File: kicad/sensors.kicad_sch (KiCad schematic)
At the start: 11 parts, among them U10 BMM350, U11 BMP581, U9 ICM-45686

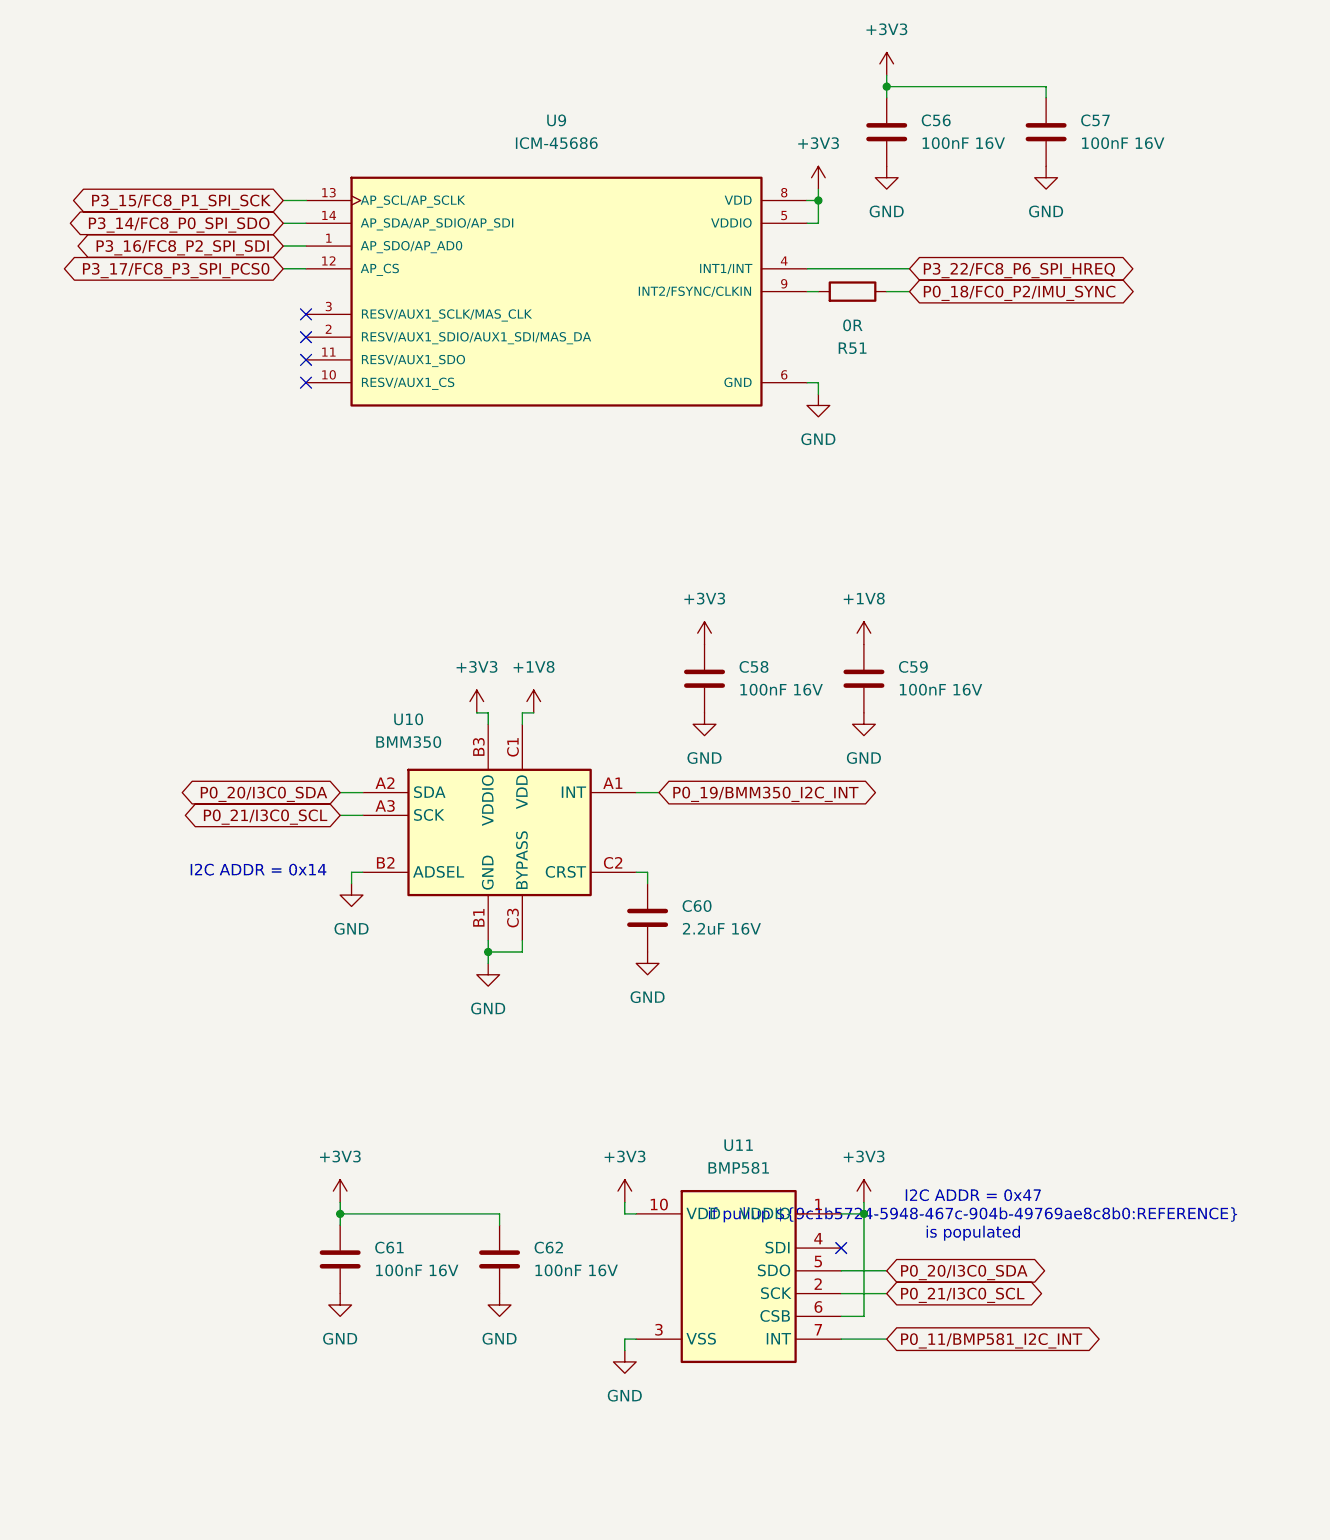
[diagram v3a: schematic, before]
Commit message: Finished schematic. Completed power and ENET phy layout.
Layouted power supply and ethernet phy around input connector.
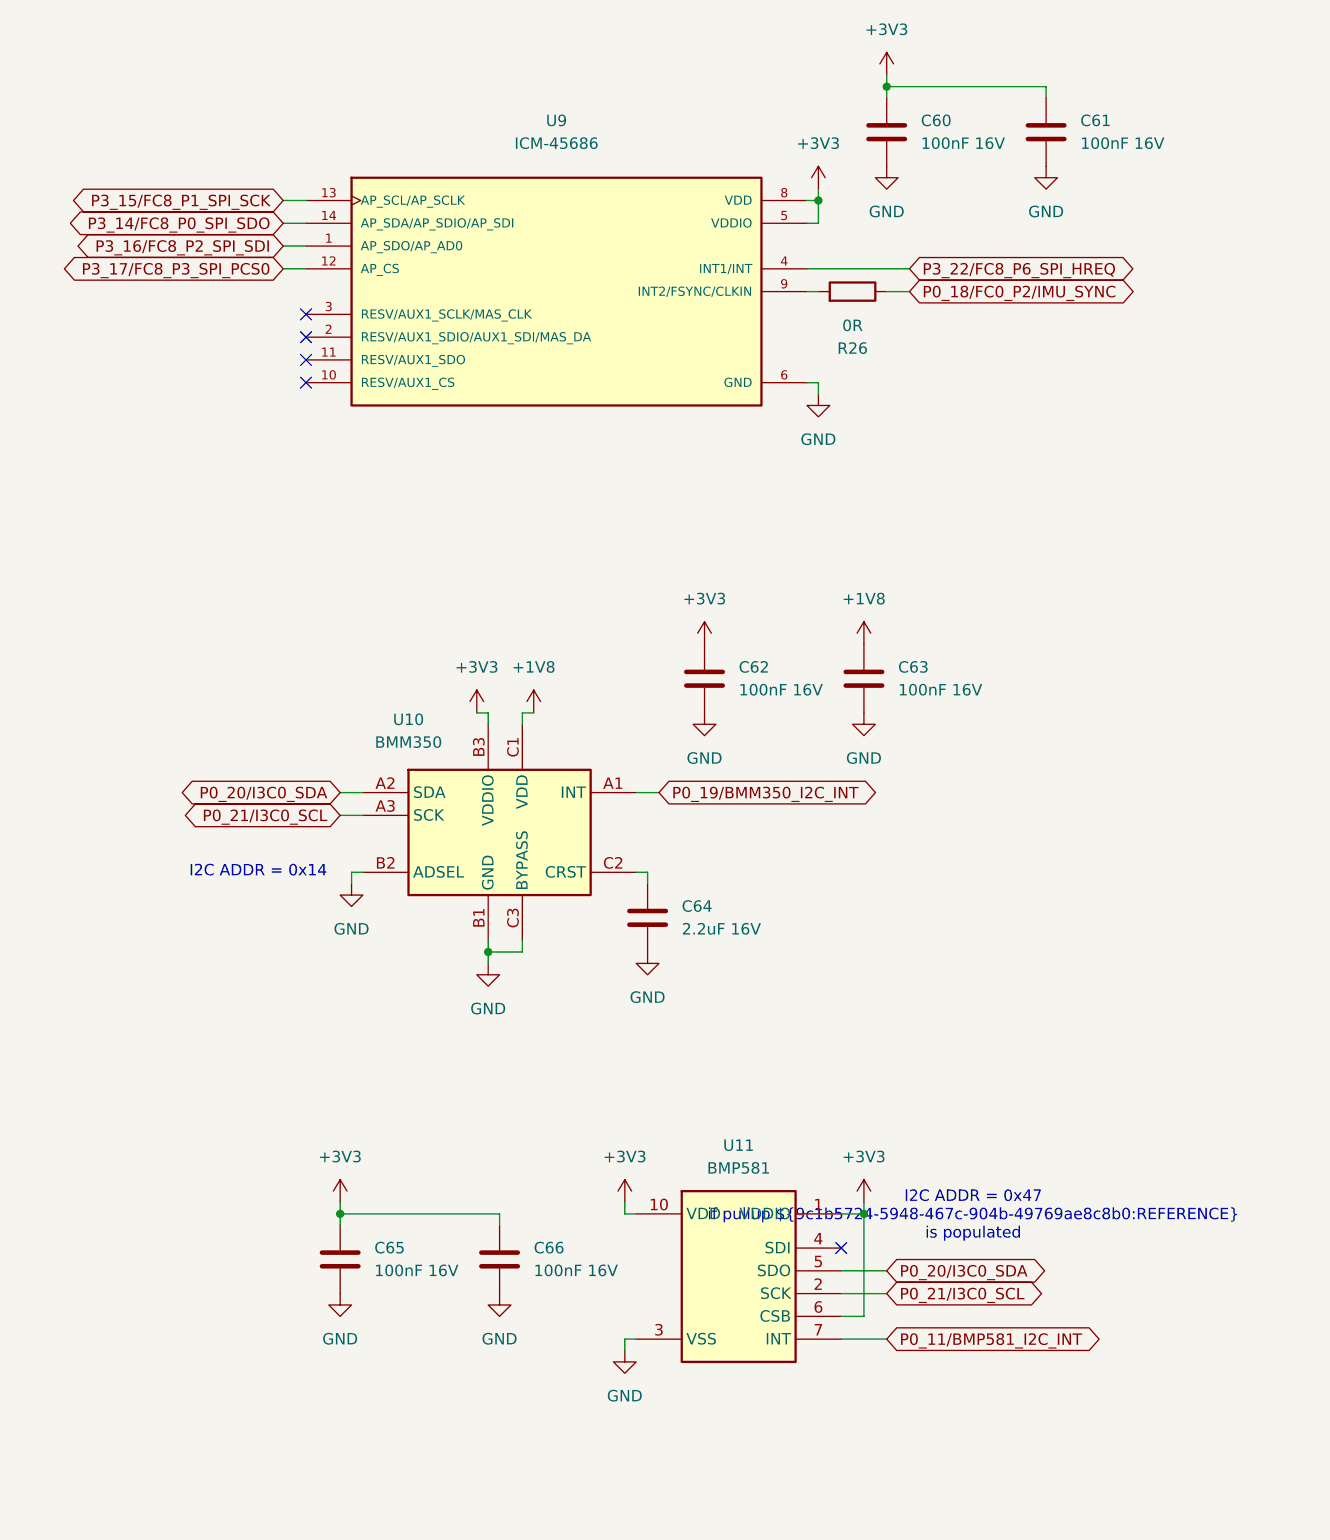
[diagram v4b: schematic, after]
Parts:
- R26: renamed from R51; footprint (none) -> Resistor_SMD:R_0402_1005Metric; MF (none) -> YAGEO; MFPN (none) -> RC0402JR-070RL; Supplier (none) -> JLCPCB; Supplier PN (none) -> C60485
- renumbered C56 to C60, C57 to C61, C58 to C62, C59 to C63, C60 to C64, C61 to C65, C62 to C66
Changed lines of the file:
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@@
 		(dnp no)
 		(fields_autoplaced yes)
-		(property "Reference" "#PWR0119"
+		(property "Reference" "#PWR0121"
 			(at 88.9 162.56 0)
 			(effects
@@
 			(project ""
 				(path "/8b469ec1-e800-4d46-8a32-95d77ceae6db/a28c0fd8-aeac-4bef-8f3f-cec5db09a131"
-					(reference "#PWR0119")
+					(reference "#PWR0121")
 					(unit 1)
 				)
@@
 		(dnp no)
 		(fields_autoplaced yes)
-		(property "Reference" "#PWR0105"
+		(property "Reference" "#PWR0107"
 			(at 118.11 49.53 0)
 			(effects
@@
 			(project "spinali_mcxn_t1_sensor_hub"
 				(path "/8b469ec1-e800-4d46-8a32-95d77ceae6db/a28c0fd8-aeac-4bef-8f3f-cec5db09a131"
-					(reference "#PWR0105")
+					(reference "#PWR0107")
 					(unit 1)
 				)
@@
 		(dnp no)
 		(fields_autoplaced yes)
-		(property "Reference" "#PWR0107"
+		(property "Reference" "#PWR0109"
 			(at 110.49 49.53 0)
 			(effects
@@
 			(project ""
 				(path "/8b469ec1-e800-4d46-8a32-95d77ceae6db/a28c0fd8-aeac-4bef-8f3f-cec5db09a131"
-					(reference "#PWR0107")
+					(reference "#PWR0109")
 					(unit 1)
 				)
@@
 		(dnp no)
 		(fields_autoplaced yes)
-		(property "Reference" "#PWR0116"
+		(property "Reference" "#PWR0118"
 			(at 91.44 137.16 0)
 			(effects
@@
 			(project "spinali_mcxn_t1_sensor_hub"
 				(path "/8b469ec1-e800-4d46-8a32-95d77ceae6db/a28c0fd8-aeac-4bef-8f3f-cec5db09a131"
-					(reference "#PWR0116")
+					(reference "#PWR0118")
 					(unit 1)
 				)
@@
 		(dnp no)
 		(fields_autoplaced yes)
-		(property "Reference" "#PWR0108"
+		(property "Reference" "#PWR0110"
 			(at 110.49 74.93 0)
 			(effects
@@
 			(project "spinali_mcxn_t1_sensor_hub"
 				(path "/8b469ec1-e800-4d46-8a32-95d77ceae6db/a28c0fd8-aeac-4bef-8f3f-cec5db09a131"
-					(reference "#PWR0108")
+					(reference "#PWR0110")
 					(unit 1)
 				)
@@
 		(dnp no)
 		(fields_autoplaced yes)
-		(property "Reference" "C60"
+		(property "Reference" "C64"
 			(at 95.25 125.7299 0)
 			(effects
@@
 			(project "spinali_mcxn_t1_sensor_hub"
 				(path "/8b469ec1-e800-4d46-8a32-95d77ceae6db/a28c0fd8-aeac-4bef-8f3f-cec5db09a131"
-					(reference "C60")
+					(reference "C64")
 					(unit 1)
 				)
@@
 		(dnp no)
 		(fields_autoplaced yes)
-		(property "Reference" "C59"
+		(property "Reference" "C63"
 			(at 119.38 99.0599 0)
 			(effects
@@
 			(project "spinali_mcxn_t1_sensor_hub"
 				(path "/8b469ec1-e800-4d46-8a32-95d77ceae6db/a28c0fd8-aeac-4bef-8f3f-cec5db09a131"
-					(reference "C59")
+					(reference "C63")
 					(unit 1)
 				)
@@
 		(dnp no)
 		(fields_autoplaced yes)
-		(property "Reference" "C57"
+		(property "Reference" "C61"
 			(at 139.7 38.0999 0)
 			(effects
@@
 			(project "spinali_mcxn_t1_sensor_hub"
 				(path "/8b469ec1-e800-4d46-8a32-95d77ceae6db/a28c0fd8-aeac-4bef-8f3f-cec5db09a131"
-					(reference "C57")
+					(reference "C61")
 					(unit 1)
 				)
@@
 		(dnp no)
 		(fields_autoplaced yes)
-		(property "Reference" "#PWR0113"
+		(property "Reference" "#PWR0115"
 			(at 97.79 110.49 0)
 			(effects
@@
 			(project "spinali_mcxn_t1_sensor_hub"
 				(path "/8b469ec1-e800-4d46-8a32-95d77ceae6db/a28c0fd8-aeac-4bef-8f3f-cec5db09a131"
-					(reference "#PWR0113")
+					(reference "#PWR0115")
 					(unit 1)
 				)
@@
 		(dnp no)
 		(fields_autoplaced yes)
-		(property "Reference" "#PWR0106"
+		(property "Reference" "#PWR0108"
 			(at 135.89 49.53 0)
 			(effects
@@
 			(project "spinali_mcxn_t1_sensor_hub"
 				(path "/8b469ec1-e800-4d46-8a32-95d77ceae6db/a28c0fd8-aeac-4bef-8f3f-cec5db09a131"
-					(reference "#PWR0106")
+					(reference "#PWR0108")
 					(unit 1)
 				)
@@
 		(dnp no)
 		(fields_autoplaced yes)
-		(property "Reference" "#PWR0114"
+		(property "Reference" "#PWR0116"
 			(at 115.57 110.49 0)
 			(effects
@@
 			(project "spinali_mcxn_t1_sensor_hub"
 				(path "/8b469ec1-e800-4d46-8a32-95d77ceae6db/a28c0fd8-aeac-4bef-8f3f-cec5db09a131"
-					(reference "#PWR0114")
+					(reference "#PWR0116")
 					(unit 1)
 				)
@@
 		(on_board yes)
 		(dnp no)
-		(property "Reference" "R51"
+		(property "Reference" "R26"
 			(at 114.3 63.5 90)
 			(effects
@@
 			)
 		)
-		(property "Footprint" ""
+		(property "Footprint" "Resistor_SMD:R_0402_1005Metric"
 			(at 114.3 58.928 90)
 			(effects
@@
 			)
 		)
+		(property "MF" "YAGEO"
+			(at 114.3 57.15 0)
+			(effects
+				(font
+					(size 1.27 1.27)
+				)
+				(hide yes)
+			)
+		)
+		(property "MFPN" "RC0402JR-070RL"
+			(at 114.3 57.15 0)
+			(effects
+				(font
+					(size 1.27 1.27)
+				)
+				(hide yes)
+			)
+		)
+		(property "Supplier" "JLCPCB"
+			(at 114.3 57.15 0)
+			(effects
+				(font
+					(size 1.27 1.27)
+				)
+				(hide yes)
+			)
+		)
+		(property "Supplier PN" "C60485"
+			(at 114.3 57.15 0)
+			(effects
+				(font
+					(size 1.27 1.27)
+				)
+				(hide yes)
+			)
+		)
 		(pin "2"
 		)
@@
 			(project ""
 				(path "/8b469ec1-e800-4d46-8a32-95d77ceae6db/a28c0fd8-aeac-4bef-8f3f-cec5db09a131"
-					(reference "R51")
+					(reference "R26")
 					(unit 1)
 				)
@@
 		(dnp no)
 		(fields_autoplaced yes)
-		(property "Reference" "C62"
+		(property "Reference" "C66"
 			(at 78.74 163.8299 0)
 			(effects
@@
 			(project ""
 				(path "/8b469ec1-e800-4d46-8a32-95d77ceae6db/a28c0fd8-aeac-4bef-8f3f-cec5db09a131"
-					(reference "C62")
+					(reference "C66")
 					(unit 1)
 				)
@@
 		(dnp no)
 		(fields_autoplaced yes)
-		(property "Reference" "#PWR0109"
+		(property "Reference" "#PWR0113"
 			(at 72.39 107.95 0)
 			(effects
@@
 			(project ""
 				(path "/8b469ec1-e800-4d46-8a32-95d77ceae6db/a28c0fd8-aeac-4bef-8f3f-cec5db09a131"
-					(reference "#PWR0109")
+					(reference "#PWR0113")
 					(unit 1)
 				)
@@
 		(dnp no)
 		(fields_autoplaced yes)
-		(property "Reference" "#PWR0120"
+		(property "Reference" "#PWR0122"
 			(at 115.57 162.56 0)
 			(effects
@@
 			(project ""
 				(path "/8b469ec1-e800-4d46-8a32-95d77ceae6db/a28c0fd8-aeac-4bef-8f3f-cec5db09a131"
-					(reference "#PWR0120")
+					(reference "#PWR0122")
 					(unit 1)
 				)
@@
 		(on_board yes)
 		(dnp no)
-		(property "Reference" "C61"
+		(property "Reference" "C65"
 			(at 60.96 163.8299 0)
 			(effects
@@
 			(project "spinali_mcxn_t1_sensor_hub"
 				(path "/8b469ec1-e800-4d46-8a32-95d77ceae6db/a28c0fd8-aeac-4bef-8f3f-cec5db09a131"
-					(reference "C61")
+					(reference "C65")
 					(unit 1)
 				)
@@
 		(dnp no)
 		(fields_autoplaced yes)
-		(property "Reference" "#PWR0117"
+		(property "Reference" "#PWR0119"
 			(at 73.66 138.43 0)
 			(effects
@@
 			(project "spinali_mcxn_t1_sensor_hub"
 				(path "/8b469ec1-e800-4d46-8a32-95d77ceae6db/a28c0fd8-aeac-4bef-8f3f-cec5db09a131"
-					(reference "#PWR0117")
+					(reference "#PWR0119")
 					(unit 1)
 				)
@@
 		(dnp no)
 		(fields_autoplaced yes)
-		(property "Reference" "#PWR0121"
+		(property "Reference" "#PWR0123"
 			(at 57.15 175.26 0)
 			(effects
@@
 			(project "spinali_mcxn_t1_sensor_hub"
 				(path "/8b469ec1-e800-4d46-8a32-95d77ceae6db/a28c0fd8-aeac-4bef-8f3f-cec5db09a131"
-					(reference "#PWR0121")
+					(reference "#PWR0123")
 					(unit 1)
 				)
@@
 		(dnp no)
 		(fields_autoplaced yes)
-		(property "Reference" "#PWR0104"
+		(property "Reference" "#PWR0106"
 			(at 118.11 36.83 0)
 			(effects
@@
 			(project "spinali_mcxn_t1_sensor_hub"
 				(path "/8b469ec1-e800-4d46-8a32-95d77ceae6db/a28c0fd8-aeac-4bef-8f3f-cec5db09a131"
-					(reference "#PWR0104")
+					(reference "#PWR0106")
 					(unit 1)
 				)
@@
 		(dnp no)
 		(fields_autoplaced yes)
-		(property "Reference" "#PWR0122"
+		(property "Reference" "#PWR0124"
 			(at 74.93 175.26 0)
 			(effects
@@
 			(project ""
 				(path "/8b469ec1-e800-4d46-8a32-95d77ceae6db/a28c0fd8-aeac-4bef-8f3f-cec5db09a131"
-					(reference "#PWR0122")
+					(reference "#PWR0124")
 					(unit 1)
 				)
@@
 		(dnp no)
 		(fields_autoplaced yes)
-		(property "Reference" "#PWR0124"
+		(property "Reference" "#PWR0125"
 			(at 88.9 181.61 0)
 			(effects
@@
 			(project "spinali_mcxn_t1_sensor_hub"
 				(path "/8b469ec1-e800-4d46-8a32-95d77ceae6db/a28c0fd8-aeac-4bef-8f3f-cec5db09a131"
-					(reference "#PWR0124")
+					(reference "#PWR0125")
 					(unit 1)
 				)
@@
 		(dnp no)
 		(fields_autoplaced yes)
-		(property "Reference" "#PWR0115"
+		(property "Reference" "#PWR0117"
 			(at 58.42 129.54 0)
 			(effects
@@
 			(project "spinali_mcxn_t1_sensor_hub"
 				(path "/8b469ec1-e800-4d46-8a32-95d77ceae6db/a28c0fd8-aeac-4bef-8f3f-cec5db09a131"
-					(reference "#PWR0115")
+					(reference "#PWR0117")
 					(unit 1)
 				)
@@
 		(dnp no)
 		(fields_autoplaced yes)
-		(property "Reference" "#PWR0110"
+		(property "Reference" "#PWR0114"
 			(at 78.74 107.95 0)
 			(effects
@@
 			(project "spinali_mcxn_t1_sensor_hub"
 				(path "/8b469ec1-e800-4d46-8a32-95d77ceae6db/a28c0fd8-aeac-4bef-8f3f-cec5db09a131"
-					(reference "#PWR0110")
+					(reference "#PWR0114")
 					(unit 1)
 				)
@@
 		(dnp no)
 		(fields_autoplaced yes)
-		(property "Reference" "C58"
+		(property "Reference" "C62"
 			(at 101.6 99.0599 0)
 			(effects
@@
 			(project "spinali_mcxn_t1_sensor_hub"
 				(path "/8b469ec1-e800-4d46-8a32-95d77ceae6db/a28c0fd8-aeac-4bef-8f3f-cec5db09a131"
-					(reference "C58")
+					(reference "C62")
 					(unit 1)
 				)
@@
 		(dnp no)
 		(fields_autoplaced yes)
-		(property "Reference" "#PWR0118"
+		(property "Reference" "#PWR0120"
 			(at 57.15 162.56 0)
 			(effects
@@
 			(project "spinali_mcxn_t1_sensor_hub"
 				(path "/8b469ec1-e800-4d46-8a32-95d77ceae6db/a28c0fd8-aeac-4bef-8f3f-cec5db09a131"
-					(reference "#PWR0118")
+					(reference "#PWR0120")
 					(unit 1)
 				)
@@
 		(dnp no)
 		(fields_autoplaced yes)
-		(property "Reference" "C56"
+		(property "Reference" "C60"
 			(at 121.92 38.0999 0)
 			(effects
@@
 			(project "spinali_mcxn_t1_sensor_hub"
 				(path "/8b469ec1-e800-4d46-8a32-95d77ceae6db/a28c0fd8-aeac-4bef-8f3f-cec5db09a131"
-					(reference "C56")
-					(unit 1)
-				)
+					(reference "C60")
+					(unit 1)
+				)

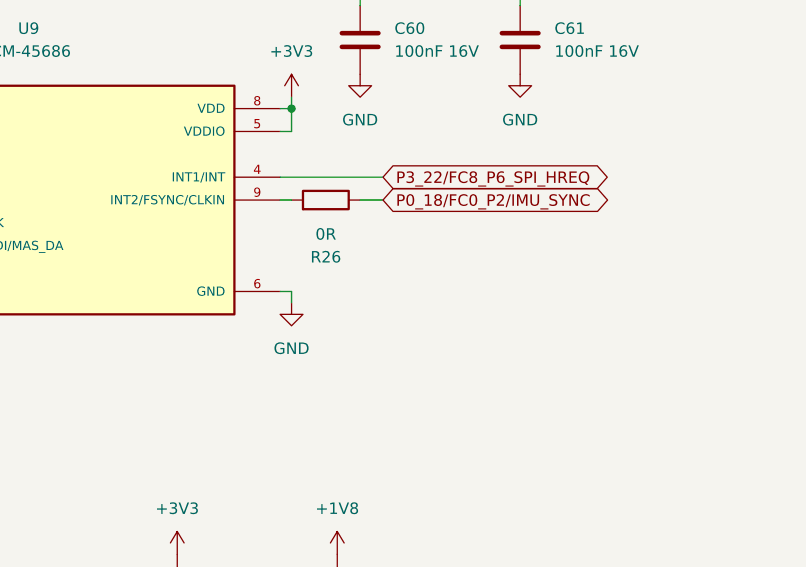
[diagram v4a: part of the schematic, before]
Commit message: Updated PCB layout
Implemented feedback:
- Placed ENET LEDs next to each other
- Added solder pads to output of RGB LED
- Made hole to hole distance in X-axis to 30.5mm
- Placed IMU a bit closer to the middle to still comply to the design rules by TDK.
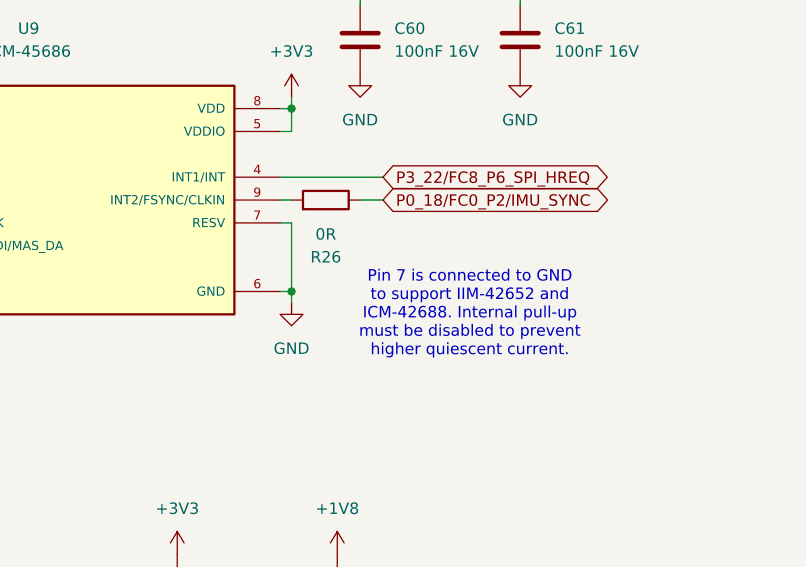
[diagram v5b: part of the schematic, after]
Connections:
- net GND: now also U9.7 (RESV)
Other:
- note added: "Pin 7 is connected to GND to support IIM-42652 and ICM-42688. Internal pull-up must be disabled to prevent higher quiescent current."
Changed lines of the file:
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@@
+	)
+	(junction
+		(at 110.49 67.31)
+		(diameter 0)
+		(color 0 0 0 0)
 	)
 	(junction
@@
 	(wire
 		(pts
+			(xy 109.22 59.69) (xy 110.49 59.69)
+		)
+		(stroke
+			(width 0)
+			(type default)
+		)
+	)
+	(wire
+		(pts
 			(xy 73.66 130.81) (xy 73.66 132.08)
 		)
@@
 	(wire
 		(pts
+			(xy 110.49 59.69) (xy 110.49 67.31)
+		)
+		(stroke
+			(width 0)
+			(type default)
+		)
+	)
+	(wire
+		(pts
 			(xy 74.93 161.29) (xy 74.93 160.02)
 		)
@@
 		)
 	)
+	(text "Pin 7 is connected to GND\nto support IIM-42652 and\nICM-42688. Internal pull-up\nmust be disabled to prevent\nhigher quiescent current."
+		(exclude_from_sim no)
+		(at 130.302 69.85 0)
+		(effects
+			(font
+				(size 1.27 1.27)
+			)
+		)
+	)

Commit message: Updated layout and BOM
- Flipped Magnetometer so it is aligned with the axis of the IMU.
- Updated BOM so all parts can be sourced from DigiKey. Also added a row for JLCPCB part numbers if applicable.
- Replaced ISP button with the NanoT160AS. Added "ISP" in silkscreen at that button.
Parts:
- C60, C61, C62, C63, C65, C66: DigiKey (none) -> 490-3261-1-ND; JLCPCB (none) -> C71629; MF Samsung Electro-Mechanics -> Murata Electronics; MFPN CL05B104KO5NNNC -> GRM155R71C104KA88D; Supplier JLCPCB -> (none); Supplier PN C1525 -> (none)
- C64: DigiKey (none) -> 490-3906-1-ND; JLCPCB (none) -> C108378; MF Samsung Electro-Mechanics -> Murata Electronics; MFPN CL21B225KAFNNNE -> GRM21BR71C225KA12L; Supplier JLCPCB -> (none); Supplier PN C19110 -> (none)
- R26: DigiKey (none) -> 311-0.0JRCT-ND; JLCPCB (none) -> C60485; Supplier JLCPCB -> (none); Supplier PN C60485 -> (none)
- U10: DigiKey (none) -> 828-BMM350CT-ND; JLCPCB (none) -> C17225907; Supplier JLCPCB -> (none); Supplier PN C17225907 -> (none)
- U11: DigiKey (none) -> 828-BMP581CT-ND; JLCPCB (none) -> C5362283; Supplier JLCPCB -> (none); Supplier PN C5362283 -> (none)
- U9: DigiKey (none) -> 1428-ICM-45686CT-ND; JLCPCB (none) -> C22459454; Supplier JLCPCB -> (none); Supplier PN C22459454 -> (none)
